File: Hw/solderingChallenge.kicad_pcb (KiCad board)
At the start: 2 copper layers, 33.5 x 33.5 mm, 28 parts, among them J1 ISP, U1 ATtiny85-20SU

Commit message: feat(Hw):Added_Puya_PCB
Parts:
- removed D1: 1206, LED_SMD:LED_1206_3216Metric_Pad1.42x1.75mm_HandSolder
- removed D2: 0805, LED_SMD:LED_0805_2012Metric_Pad1.15x1.40mm_HandSolder
- removed D3: 0603, LED_SMD:LED_0603_1608Metric_Pad1.05x0.95mm_HandSolder
- removed D4: 0402, LED_SMD:LED_0402_1005Metric
- removed the G*** at (133.6, 88.9)
- removed the G*** at (133.3, 85.2)
- removed the G*** at (150.4, 88.2)
- removed the G*** at (130.4, 73.0)
- removed the G*** at (151.4, 89.1)
- removed the G*** at (137.8, 69.1)
- removed the G*** at (142.6, 92.3)
- removed the G*** at (150.2, 69.0)
- removed J1: ISP, Connector_PinHeader_2.54mm:PinHeader_2x03_P2.54mm_Vertical
- removed R1: 1206, Resistor_SMD:R_1206_3216Metric_Pad1.42x1.75mm_HandSolder
- removed R2: 0805, Resistor_SMD:R_0805_2012Metric_Pad1.15x1.40mm_HandSolder
- removed R3: 0603, Resistor_SMD:R_0603_1608Metric_Pad1.05x0.95mm_HandSolder
- removed R4: 0402, Resistor_SMD:R_0402_1005Metric
- removed TP1: PB0, TestPoint:TestPoint_Pad_1.0x1.0mm
- removed TP10, TP6, TP7, TP8: GND, Connectors_EC:TestPoint_Pad_1.0x1.0mm
- removed TP2: PB1, Connectors_EC:TestPoint_Pad_1.0x1.0mm
- removed TP3: PB2, Connectors_EC:TestPoint_Pad_1.0x1.0mm
- removed TP4: PB3, Connectors_EC:TestPoint_Pad_1.0x1.0mm
- added D5: Green, LED_SMD:LED_1206_3216Metric_Pad1.42x1.75mm_HandSolder, F.Cu at (144.1, 73.5)
- added D6: Red, LED_SMD:LED_0805_2012Metric, F.Cu at (144.1, 77.5)
- added D7: Blue, LED_SMD:LED_0603_1608Metric_Pad1.05x0.95mm_HandSolder, F.Cu at (144.1, 81.0)
- added D9: Yellow, LED_SMD:LED_0402_1005Metric_Pad0.77x0.64mm_HandSolder, F.Cu at (144.0, 83.8)
- added G***: LOGO, Aesthetics:pcbway_13x4, F.Cu at (142.4, 88.5)
- added G***: LOGO, Aesthetics:electronic_cats_logo_4x3, F.Cu at (142.5, 92.6)
- added J2: SWD, Connector_PinHeader_2.54mm:PinHeader_1x04_P2.54mm_Vertical, B.Cu at (154.8, 71.1)
- added R5: 330R, Resistor_SMD:R_1206_3216Metric_Pad1.30x1.75mm_HandSolder, F.Cu at (149.9, 73.5)
- added R6: 330R, Resistor_SMD:R_0805_2012Metric, F.Cu at (149.9, 77.5)
- added R7: 330R, Resistor_SMD:R_0603_1608Metric_Pad0.98x0.95mm_HandSolder, F.Cu at (149.9, 81.0)
- added R9: 330R, Resistor_SMD:R_0402_1005Metric_Pad0.72x0.64mm_HandSolder, F.Cu at (149.9, 83.8)
- added SW1: SW_RST, Button_Switch_SMD:SW_SPST_TL3342, B.Cu at (142.4, 72.2)
- added SW2: On, solderingChallenge:MSK12C02, F.Cu at (134.2, 67.3)
- added kibuzzard-67914DBF: G***, kibuzzard-67914DBF, F.Cu at (154.3, 73.3)
- added kibuzzard-67914DD8: G***, kibuzzard-67914DD8, F.Cu at (154.3, 77.0)
- added kibuzzard-67914DE9: G***, kibuzzard-67914DE9, F.Cu at (154.3, 80.4)
- added kibuzzard-67914E01: G***, kibuzzard-67914E01, F.Cu at (154.3, 83.6)
- added kibuzzard-67916211: G***, kibuzzard-67916211, F.Cu at (129.1, 79.0)
- added kibuzzard-6791629E: G***, kibuzzard-6791629E, F.Cu at (129.1, 79.0)
- added kibuzzard-67916383: G***, kibuzzard-67916383, B.Cu at (153.0, 73.0)
- added kibuzzard-679163A9: G***, kibuzzard-679163A9, B.Cu at (149.4, 69.4)
- added kibuzzard-679163CD: G***, kibuzzard-679163CD, B.Cu at (151.2, 71.2)
- added kibuzzard-679168C7: G***, kibuzzard-679168C7, B.Cu at (156.0, 78.8)
- added kibuzzard-679168F3: G***, kibuzzard-679168F3, B.Cu at (147.6, 67.5)
- added kibuzzard-67916B62: G***, kibuzzard-67916B62, F.Cu at (139.4, 67.8)
- BT1: footprint Connectors_EC:79523141 -> solderingChallenge:BAT-HLD-001
- C1: footprint Capacitor_SMD:C_0805_2012Metric_Pad1.15x1.40mm_HandSolder -> Capacitor_SMD:C_0805_2012Metric
- U1: value ATtiny85-20SU -> PY32F002AA15M6TU; footprint Package_SO:SOIJ-8_5.3x5.3mm_P1.27mm -> solderingChallenge:PY32F002AA15M
- moved BT1 8.02 mm to (142.5, 87.2)
- moved C1 4.05 mm to (134.6, 74.4), turned to 0 degrees
- moved U1 0.25 mm to (136.1, 78.7)
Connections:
- BT1 pad 1: VCC -> Net-(BT1--)
- BT1 pad 2: GND -> +3.3V
- C1 pad 1: VCC -> +3.3V
- U1 pad 1: /RST -> +3.3V
- U1 pad 2: /PB3 -> /PF0
- U1 pad 3: /PB4 -> /PA5
- U1 pad 4: GND -> /NRST
- U1 pad 5: /MOSI -> /PA1
- U1 pad 6: /MISO -> /PA6
- U1 pad 7: /PB2 -> /PA7
- U1 pad 8: VCC -> /SWDIO
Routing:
- net VCC: track 74.0 -> 0.00 mm, vias 2 -> 0
- net +3.3V: track 0.00 -> 59.2 mm, vias 0 -> 3
- net GND: track 44.1 -> 1.08 mm, vias 6 -> 1
- net /RST: track 39.2 -> 0.00 mm, vias 2 -> 0
- net /PB2: track 38.4 -> 0.00 mm, vias 2 -> 0
- net /MISO: track 24.8 -> 0.00 mm, vias 2 -> 0
- net /NRST: track 0.00 -> 24.7 mm, vias 0 -> 1
- net Net-(BT1--): track 0.00 -> 24.5 mm, vias 0 -> 1
- net /SWDIO: track 0.00 -> 20.9 mm, vias 0 -> 1
- net /SWCLK: track 0.00 -> 19.3 mm, vias 0 -> 1
- net /PB3: track 19.3 -> 0.00 mm
- net /MOSI: track 17.7 -> 0.00 mm, vias 2 -> 0
- net /PA5: track 0.00 -> 17.6 mm
- net /PA1: track 0.00 -> 13.1 mm
- net /PA7: track 0.00 -> 5.87 mm
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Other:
- net class Default removed
- net class vcc removed
- board text removed: "0402"
- board text removed: "0603"
- board text removed: "0805"
- board text removed: "1206"
- board text removed: "Soldering Challenge"
- board text removed: "V1.0"

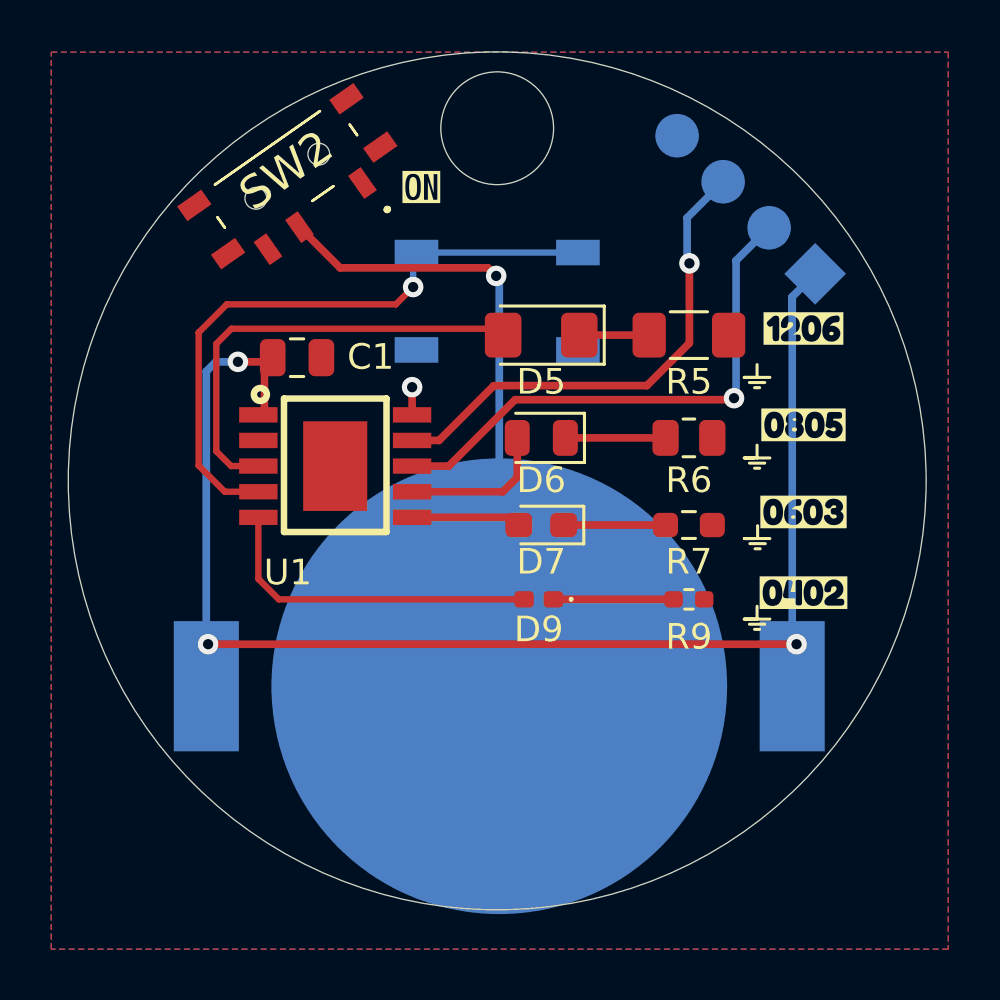
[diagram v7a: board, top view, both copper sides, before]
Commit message: feat(Hw):Align_Components
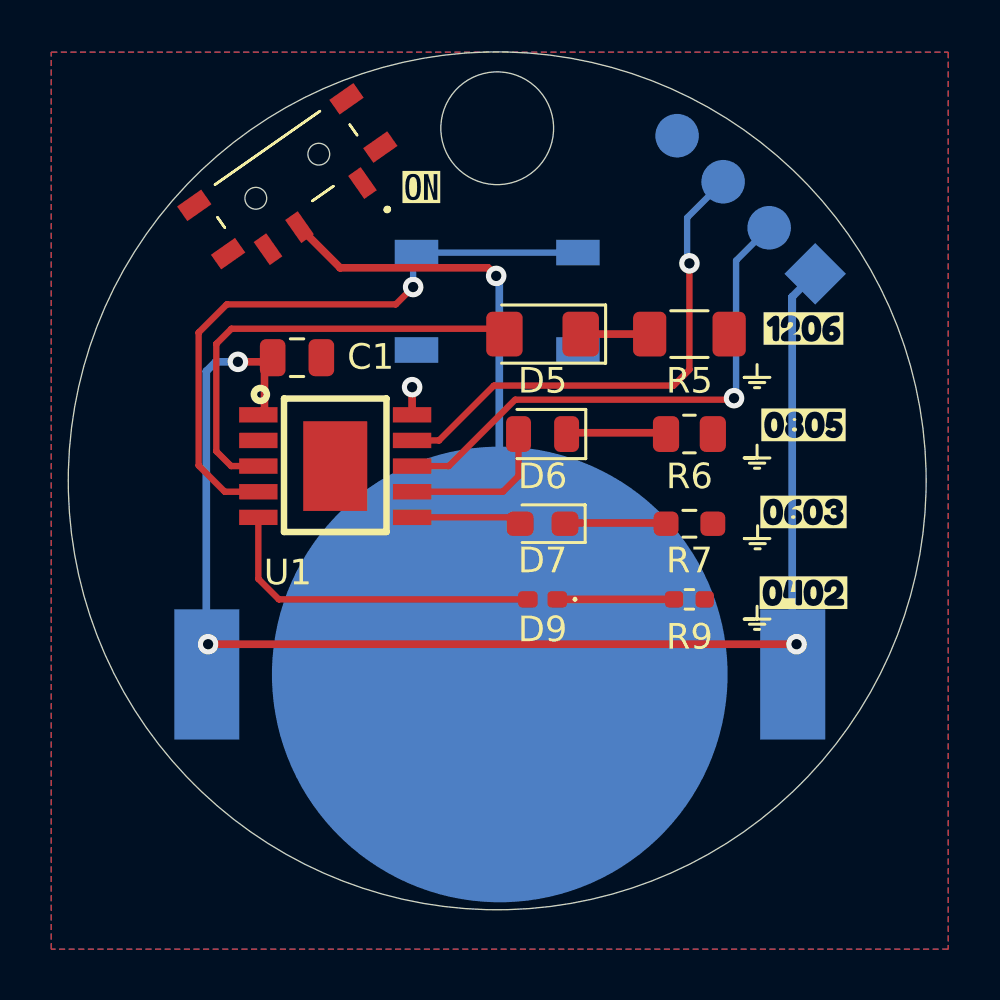
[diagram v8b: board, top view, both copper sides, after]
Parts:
- moved BT1 0.46 mm to (142.5, 86.8)
- moved D6 0.16 mm to (144.2, 77.4)
- moved R6 0.15 mm to (149.9, 77.4)
- moved D9 0.15 mm to (144.2, 83.8)
- moved D7 0.07 mm to (144.2, 80.9)
- moved D5 0.07 mm to (144.2, 73.5)
- moved R7 0.05 mm to (149.9, 80.9)
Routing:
- net +3.3V: track 59.2 -> 57.9 mm
- net /SWCLK: track 19.3 -> 19.9 mm
